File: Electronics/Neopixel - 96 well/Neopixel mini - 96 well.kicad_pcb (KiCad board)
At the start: 2 copper layers, 121.5 x 83 mm, 201 parts, among them J1 Conn_01x03_Male, J2 USB_B, U1 SAMD21_MOD

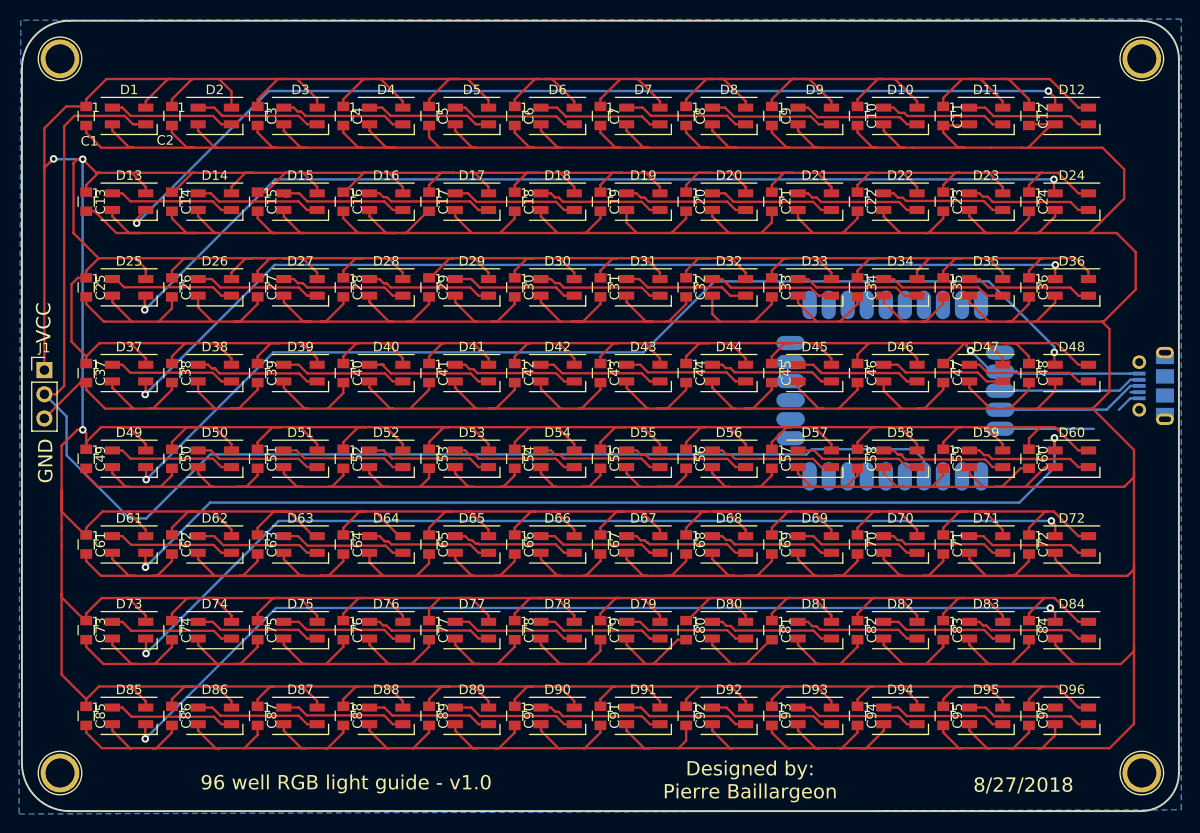
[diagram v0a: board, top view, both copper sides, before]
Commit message: Added fiducials and cleaned up silkscreen layer
Added fiducial marks to four corners of board as recommended here: http://www.ladyada.net/library/pcb/fiducials.html

Also cleaned up the silkscreen layer to properly identify pin 1 of each LED and  clean up overlapping text.
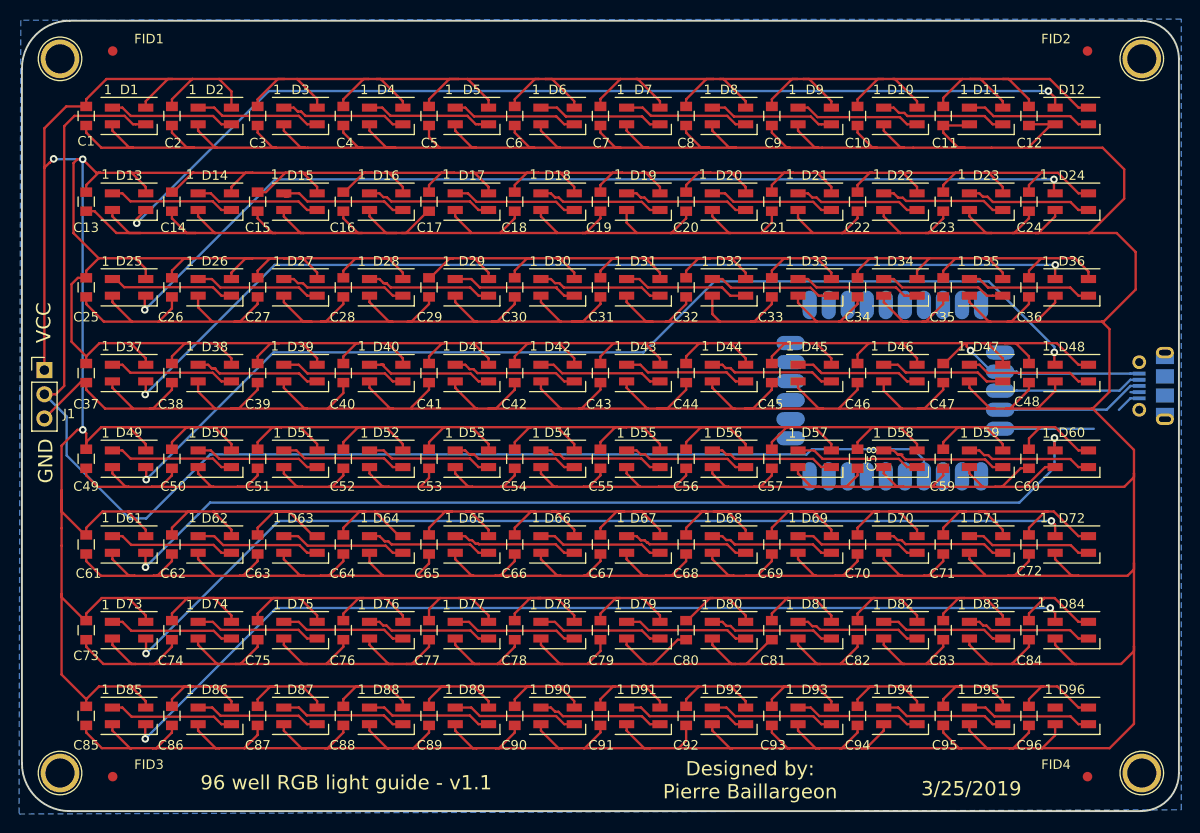
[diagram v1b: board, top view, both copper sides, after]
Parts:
- removed G***: ScrippsResearchLogo-new, LED Matrix - 96 well:ScrippsResearchLogo-new
- added FID1: Fiducial_1mm_Mask3mm, Fiducials:Fiducial_1mm_Mask3mm, F.Cu at (49.5, 43.2)
- added FID2: Fiducial_1mm_Mask3mm, Fiducials:Fiducial_1mm_Mask3mm, F.Cu at (151.9, 43.2)
- added FID3: Fiducial_1mm_Mask3mm, Fiducials:Fiducial_1mm_Mask3mm, F.Cu at (49.5, 119.4)
- added FID4: Fiducial_1mm_Mask3mm, Fiducials:Fiducial_1mm_Mask3mm, F.Cu at (151.9, 119.4)
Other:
- board text added: "3/25/2019"
- board text added: "96 well RGB light guide - v1.1"
- board text removed: "8/27/2018"
- board text removed: "96 well RGB light guide - v1.0"
